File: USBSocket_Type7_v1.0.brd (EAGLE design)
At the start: 22.7 x 15.2 mm, 8 parts, among them X1 USBPCB

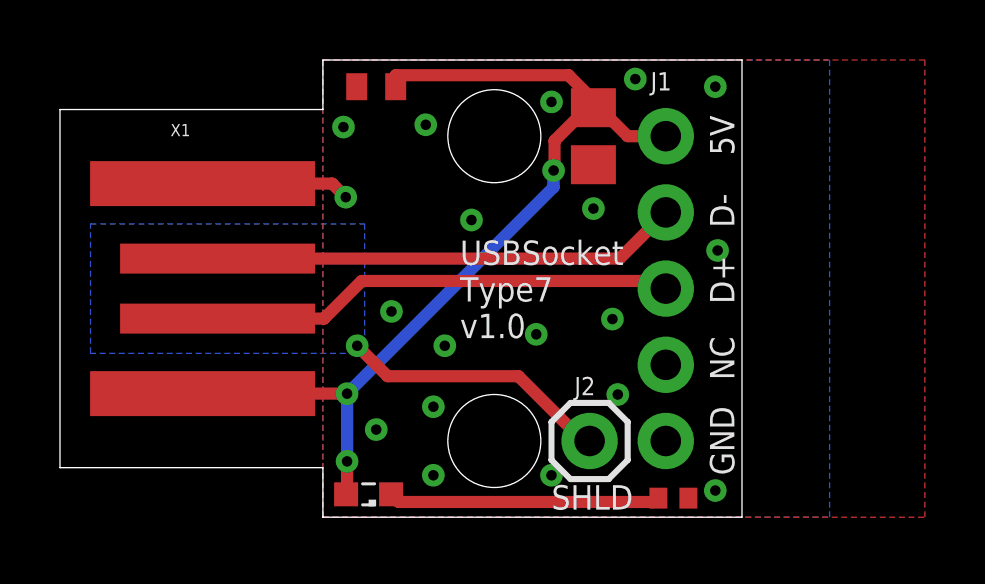
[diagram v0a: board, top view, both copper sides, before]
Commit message: Fixed schematic and routing for t7 board.
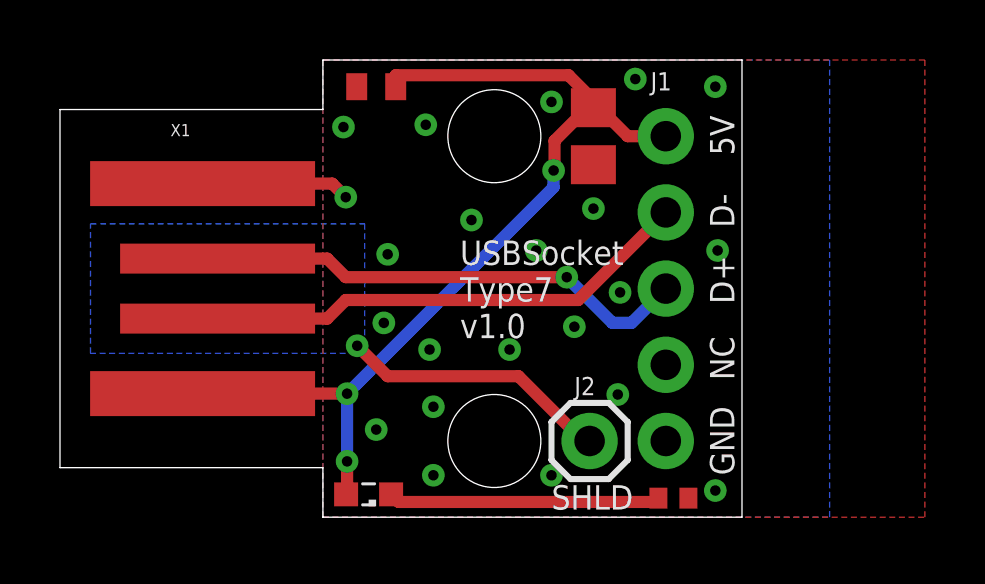
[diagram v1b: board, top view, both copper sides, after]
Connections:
- net USB_D_M: now also X1.USB_M; no longer X1.USB_P
- net USB_D_P: now also X1.USB_P; no longer X1.USB_M
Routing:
- net USB_D_M: track 15.6 -> 16.4 mm
- net USB_D_P: track 15.6 -> 16.3 mm, vias 0 -> 1
- net GND: vias 19 -> 22
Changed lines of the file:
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@@
 <drawing>
 <settings>
-<setting alwaysvectorfont="yes"/>
+<setting alwaysvectorfont="no"/>
 <setting verticaltext="up"/>
 </settings>
@@
 <via x="11.43" y="13.843" extent="1-16" drill="0.35"/>
 <via x="14.224" y="14.605" extent="1-16" drill="0.35"/>
-<via x="13.462" y="6.604" extent="1-16" drill="0.35"/>
-<via x="7.874" y="5.715" extent="1-16" drill="0.35"/>
+<via x="7.366" y="5.588" extent="1-16" drill="0.35"/>
 <via x="7.493" y="3.683" extent="1-16" drill="0.35"/>
 <via x="7.493" y="1.397" extent="1-16" drill="0.35"/>
 <via x="11.43" y="1.397" extent="1-16" drill="0.35"/>
-<via x="10.922" y="6.096" extent="1-16" drill="0.35"/>
+<via x="12.192" y="6.35" extent="1-16" drill="0.35"/>
 <contactref element="X1" pad="GND"/>
 <via x="5.588" y="2.921" extent="1-16" drill="0.35"/>
 <via x="4.572" y="10.668" extent="1-16" drill="0.35"/>
 <via x="8.763" y="9.906" extent="1-16" drill="0.35"/>
-<via x="6.096" y="6.858" extent="1-16" drill="0.35"/>
 <wire x1="-0.2" y1="11.12" x2="4.12" y2="11.12" width="0.4064" layer="1"/>
 <wire x1="4.12" y1="11.12" x2="4.572" y2="10.668" width="0.4064" layer="1"/>
+<via x="10.922" y="8.89" extent="1-16" drill="0.35"/>
+<via x="13.716" y="7.493" extent="1-16" drill="0.35"/>
+<via x="5.842" y="6.477" extent="1-16" drill="0.35"/>
+<via x="5.969" y="8.763" extent="1-16" drill="0.35"/>
+<via x="10.033" y="5.588" extent="1-16" drill="0.35"/>
 </signal>
 <signal name="5V" class="3">
@@
 <signal name="USB_D_M" class="1">
 <contactref element="J1" pad="2"/>
-<wire x1="13.7" y1="8.62" x2="15.24" y2="10.16" width="0.4064" layer="1"/>
-<contactref element="X1" pad="USB_P"/>
-<wire x1="0.3" y1="8.62" x2="13.7" y2="8.62" width="0.4064" layer="1"/>
+<contactref element="X1" pad="USB_M"/>
+<wire x1="0.3" y1="6.62" x2="3.953" y2="6.62" width="0.4064" layer="1"/>
+<wire x1="3.953" y1="6.62" x2="4.572" y2="7.239" width="0.4064" layer="1"/>
+<wire x1="4.572" y1="7.239" x2="12.319" y2="7.239" width="0.4064" layer="1"/>
+<wire x1="12.319" y1="7.239" x2="15.24" y2="10.16" width="0.4064" layer="1"/>
 </signal>
 <signal name="USB_D_P" class="1">
 <contactref element="J1" pad="3"/>
-<wire x1="15.24" y1="7.62" x2="14.986" y2="7.874" width="0.4064" layer="1"/>
-<wire x1="5.103" y1="7.874" x2="14.986" y2="7.874" width="0.4064" layer="1"/>
-<contactref element="X1" pad="USB_M"/>
-<wire x1="0.3" y1="6.62" x2="3.849" y2="6.62" width="0.4064" layer="1"/>
-<wire x1="3.849" y1="6.62" x2="5.103" y2="7.874" width="0.4064" layer="1"/>
+<contactref element="X1" pad="USB_P"/>
+<wire x1="14.097" y1="6.477" x2="15.24" y2="7.62" width="0.4064" layer="16"/>
+<wire x1="0.3" y1="8.62" x2="3.953" y2="8.62" width="0.4064" layer="1"/>
+<wire x1="3.953" y1="8.62" x2="4.572" y2="8.001" width="0.4064" layer="1"/>
+<wire x1="4.572" y1="8.001" x2="11.938" y2="8.001" width="0.4064" layer="1"/>
+<via x="11.938" y="8.001" extent="1-16" drill="0.35"/>
+<wire x1="11.938" y1="8.001" x2="13.462" y2="6.477" width="0.4064" layer="16"/>
+<wire x1="13.462" y1="6.477" x2="14.097" y2="6.477" width="0.4064" layer="16"/>
 </signal>
 <signal name="USB_SHIELD">
